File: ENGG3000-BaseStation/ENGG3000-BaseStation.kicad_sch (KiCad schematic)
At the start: 49 parts, among them J2 OLED, J3 Buttons, J4 USB_C_Receptacle_USB2.0_16P, J5 Cell 3, J6 Cell 2, J7 Cell 1, J8 CHRG LED, Q1 SS8050, Q2 AO3401A, SW1 RESET, SW2 BOOT, U1 ESP32-S3-WROOM-1-N16R8, U2 CN3085, U3 TPS63001DRCR, U5 AMS1117-3.3

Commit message: Component updates
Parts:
- removed C1: 10uF, Capacitor_SMD:C_0402_1005Metric, symbol Device:C
- removed C2, C4: 10uF, Capacitor_Tantalum_SMD:CP_EIA-3216-18_Kemet-A, symbol Device:C_Polarized
- removed R21: 1m, Resistor_SMD:R_0402_1005Metric, symbol Device:R
- removed U5: AMS1117-3.3, Package_TO_SOT_SMD:SOT-223-3_TabPin2, symbol Regulator_Linear:AMS1117-3.3
- added C10: 100nF, Capacitor_SMD:C_0402_1005Metric, symbol Device:C
- added C8, C9: 10uF, Capacitor_Tantalum_SMD:CP_EIA-3216-18_Kemet-A, symbol Device:C_Polarized
- added L1: L, Inductor_SMD:L_APV_ANR4020, symbol Device:L
- added R22: 100R, Resistor_SMD:R_0402_1005Metric, symbol Device:R
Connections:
- net +3.3V: now also U3.1 (VOUT), U3.10 (FB), C8.1, C9.1
- net GND: now also U3.11 (PGND), U3.3 (PGND), U3.9 (GND), C10.2, C8.2, C9.2
- net at U3.2 (L2): now also L1.1
- net at U3.4 (L1): now also L1.2
- net VIN: now reaches U3.5 (VIN)
- net VIN: now also R22.2
- net at U3.6 (EN): now also U3.7 (PS/SYNC), U3.8 (VINA), C10.1, R22.1
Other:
- moved on the sheet: BZ1, C3, D1, D2, D3, J2, J3, Q1, Q2, R10, R11, R12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

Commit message: Updated power path
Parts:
- added D5, D6: SS14, Diode_SMD:D_SMA, symbol Diode:SS14
- added J9: Power Switch, Connector_JST:JST_XH_B2B-XH-A_1x02_P2.50mm_Vertical, symbol Connector:Conn_01x02_Socket
- added R21: 1k, Resistor_SMD:R_0402_1005Metric, symbol Device:R
- added R23: 10k, Resistor_SMD:R_0402_1005Metric, symbol Device:R
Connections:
- net +5V: now also D6.2 (A), R21.2
- net GND: now also R23.1
- net VIN: now also D5.1 (K), D6.1 (K)
- net at C10.1, R22.1, U3.7 (PS/SYNC)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: now also J9.1 (-); no longer U3.6 (EN)
- net at Q2.1 (G): now also R21.1, R23.2
- net LATCH: no longer names the net of Q2.3 (D)
- net LATCH: now also D5.2 (A)
- new net: J9.2 (+), U3.6 (EN)
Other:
- note added: "BaseStation"
- note added: "Power path"
- note added: "Switching regulator for 3.3v"
- note removed: "Motor Driver Controller"
- moved on the sheet: BZ1, C10, C8, C9, J4, L1, Q1, Q2, R1, R2, R20, R22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

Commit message: Update to schematic
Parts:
- removed D5: SS14, Diode_SMD:D_SMA, symbol Diode:SS14
- removed J5: Cell 3, Connector_JST:JST_XH_B2B-XH-A_1x02_P2.50mm_Vertical, symbol Connector:Conn_01x02_Socket
- removed J9: Power Switch, Connector_JST:JST_XH_B2B-XH-A_1x02_P2.50mm_Vertical, symbol Connector:Conn_01x02_Socket
- removed R16: 20k, Resistor_SMD:R_0402_1005Metric, symbol Device:R
- added C8: 1uF, Capacitor_SMD:C_0402_1005Metric, symbol Device:C
- added D2: SS14, Diode_SMD:D_SMA, symbol Diode:SS14
- added J4: Power Switch, Connector_PinHeader_2.54mm:PinHeader_1x02_P2.54mm_Vertical, symbol Connector:Conn_01x02_Socket
- added J8: UltrasonicA, Connector_PinHeader_2.54mm:PinHeader_1x04_P2.54mm_Vertical, symbol Connector:Conn_01x04_Socket
- added J9: UltrasonicB, Connector_PinHeader_2.54mm:PinHeader_1x04_P2.54mm_Vertical, symbol Connector:Conn_01x04_Socket
- added R6: 10k, Resistor_SMD:R_0402_1005Metric, symbol Device:R
- J5: renamed from J2; footprint Connector_JST:JST_XH_B4B-XH-A_1x04_P2.50mm_Vertical -> Connector_PinHeader_2.54mm:PinHeader_1x04_P2.54mm_Vertical
- J6: renamed from J3; footprint (none) -> Connector_PinHeader_2.54mm:PinHeader_1x05_P2.54mm_Vertical
- L1: value L -> 2.2uH
- UART1: renamed from UART0; footprint Connector_JST:JST_XH_B4B-XH-A_1x04_P2.50mm_Vertical -> Connector_PinHeader_2.54mm:PinHeader_1x04_P2.54mm_Vertical
- renumbered C5 to C1, C3 to C2, C6 to C3, C7 to C4, C10 to C5, C9 to C6, C8 to C7, D4 to D1, D6 to D3, D1 to D4, D2 to D5, D3 to D6, J8 to J1, J6 to J2, J7 to J3, J4 to J7, Q2 to Q1, Q1 to Q2, R13 to R1, R23 to R11, R3 to R12, R11 to R13, R21 to R14, R12 to R15, R4 to R16, R22 to R17, R20 to R18, R5 to R19, R14 to R2, R1 to R20, R2 to R21, R6 to R22, R7 to R23, R8 to R3, R19 to R4, R18 to R5, R17 to R7, R15 to R8, U2 to U1, U1 to U2
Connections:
- net +3.3V: now also C8.1, J8.4 (3.3V), J9.4 (3.3V)
- net BAT: now also J2.2 (+), D2.2 (A), R6.1; no longer Q1.2 (S)
- net FB: now also R6.2
- net GND: now also C8.2, J8.1 (GND), J9.1 (GND)
- net VIN: now also J4.1 (-); no longer D3.1 (K)
- net at U3.6 (EN): now also C5.1, R17.1, U3.7 (PS/SYNC), U3.8 (VINA)
- net Ass: now reaches R23.1
- net at Q1.3 (D): now also D3.1 (K), J4.2 (+)
- new net: D2.1 (K), Q1.2 (S)
- new net GPIO12: J8.2 (TRIG)
- new net GPIO14: J8.3 (ECHO)
- new net GPIO26: J9.3 (ECHO)
- new net GPIO27: J9.2 (TRIG)
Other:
- note added: "USB-C IN"
- moved on the sheet: BZ1, D3, J7, L1, Q2, R10, R18, R20, R21, SW2

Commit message: Sensor Calibration
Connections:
- net Ass is gone; now on net GPIO14: R23.1
- net GPIO12 is gone; now on net GPIO1: J8.2 (TRIG)
- net GPIO26 is gone; now on net GPIO13: J9.3 (ECHO)
- net GPIO27 is gone; now on net GPIO4: J9.2 (TRIG)
- net GPIO14: now also U2.22 (GPIO14/TOUCH14/ADC2_CH3/FSPIWP/FSPIDQS/SUBSPIWP); no longer J8.3 (ECHO)
- net GPIO6: now reaches J6.2 (Button_A)
- net GPIO6: now also U2.6 (GPIO6/TOUCH6/ADC1_CH5)
- net GPIO7: now reaches J6.3 (Button_B)
- net GPIO7: now also U2.7 (GPIO7/TOUCH7/ADC1_CH6)
- net GPIO10: now reaches J6.4 (Button_C)
- net GPIO10: now also U2.18 (GPIO10/TOUCH10/ADC1_CH9/FSPICS0/FSPIIO4/SUBSPICS0)
- net GPIO11: now reaches J6.5 (Button_D)
- net GPIO11: now also U2.19 (GPIO11/TOUCH11/ADC2_CH0/FSPID/FSPIIO5/SUBSPID)
- net GPIO17: now reaches R18.1
- net GPIO17: now also U2.10 (GPIO17/U1TXD/ADC2_CH6)
- net GPIO3: now reaches U2.15 (GPIO3/TOUCH3/ADC1_CH2)
- net GPIO3: now also J8.3 (ECHO)
- net GPIO13: now reaches U2.21 (GPIO13/TOUCH13/ADC2_CH2/FSPIQ/FSPIIO7/SUBSPIQ)
- net GPIO1: now reaches U2.39 (GPIO1/TOUCH1/ADC1_CH0)
- net GPIO4: now reaches U2.4 (GPIO4/TOUCH4/ADC1_CH3)
- no-connect marks 5 -> 8

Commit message: Kicad footprint update
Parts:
- removed C4: 10uF, Capacitor_SMD:C_0402_1005Metric, symbol Device:C
- removed D2: SS14, Diode_SMD:D_SMA, symbol Diode:SS14
- removed J1: CHRG LED, Connector_JST:JST_XH_B2B-XH-A_1x02_P2.50mm_Vertical, symbol Connector:Conn_01x02_Socket
- removed R7: 10k, Resistor_SMD:R_0402_1005Metric, symbol Device:R
- removed R8: 5.1k, Resistor_SMD:R_0402_1005Metric, symbol Device:R
- added C5, C9: 10uF, Capacitor_SMD:C_0805_2012Metric, symbol Device:C
- added J8: Cell 3, Connector_JST:JST_XH_B2B-XH-A_1x02_P2.50mm_Vertical, symbol Connector:Conn_01x02_Socket
- added JP1, JP2: SolderJumper, Jumper:SolderJumper-2_P1.3mm_Bridged2Bar_RoundedPad1.0x1.5mm, symbol Jumper:SolderJumper_2_Bridged
- added R23: 10k, Resistor_SMD:R_0805_2012Metric_Pad1.20x1.40mm_HandSolder, symbol Device:R
- C8: renamed from C3; footprint Capacitor_SMD:C_0402_1005Metric -> Capacitor_SMD:C_0805_2012Metric; LCSC part C15525 -> C15850
- D5: renamed from D3; LCSC part (none) -> C2480
- J10: renamed from J3; value Cell 1 -> Cell/Pack 1
- R20: renamed from R6; footprint Resistor_SMD:R_0402_1005Metric -> Resistor_SMD:R_0805_2012Metric_Pad1.20x1.40mm_HandSolder; LCSC part C25744 -> C17414
- renumbered C2 to C1, C6 to C2, C7 to C3, C8 to C4, C5 to C6, C1 to C7, D4 to D1, D5 to D2, D6 to D3, D1 to D4, J5 to J1, J6 to J2, J8 to J3, J9 to J4, J7 to J5, J4 to J7, J2 to J9, Q2 to Q1, Q1 to Q2, R3 to R1, R20 to R10, R21 to R11, R18 to R12, R17 to R13, R4 to R14, R5 to R15, R9 to R17, R11 to R18, R1 to R19, R19 to R2, R14 to R21, R2 to R22, R22 to R3, R23 to R4, R12 to R5, R16 to R6, R10 to R7, R13 to R8, R15 to R9, U2 to U1, U3 to U2, U1 to U3
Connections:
- net +5V: now also R21.1; no longer R21.2
- net BAT: now also Q2.3 (D), J8.2 (+), JP1.1 (A); no longer J9.2 (+)
- net FB: now also R23.1
- net GND: now also C5.2, C9.2, R23.2
- net VIN: now also C5.1
- net at D5.1 (K), J7.2 (+): now also Q2.2 (S); no longer Q2.3 (D)
- net at Q2.1 (G), R18.2: now also R21.2; no longer R21.1
- net at R15.2, U3.6 (RC): now also C9.1
- net at J10.2 (+), J9.1 (-): now also JP2.1 (A)
- new net: J8.1 (-), J9.2 (+), JP1.2 (B), JP2.2 (B)
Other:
- moved on the sheet: C6, D5, J10, J7, J9, Q2, R13, R18, R21

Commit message: PCB footprint addition and Calibration graphs added
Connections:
- net +3.3V: now also BZ1.1 (+)
- net +5V: no longer BZ1.1 (+)
- net GPIO1: now also J2.2 (Button_A); no longer J3.2 (TRIG)
- net GPIO10: now also J4.3 (ECHO); no longer J2.4 (Button_C)
- net GPIO11: now also J3.3 (ECHO); no longer J2.5 (Button_D)
- net GPIO13: now also J3.2 (TRIG); no longer J4.3 (ECHO)
- net GPIO3: now also J4.2 (TRIG); no longer J3.3 (ECHO)
- net GPIO48: now reaches U1.25 (GPIO48/SPICLK_N/SUBSPICLK_N_DIFF)
- net GPIO48: now also R4.1
- net GPIO40: now reaches U1.33 (MTDO/GPIO40/CLK_OUT2)
- net GPIO40: now also J2.5 (Button_D)
- net GPIO41: now reaches U1.34 (MTDI/GPIO41/CLK_OUT1)
- net GPIO41: now also J2.4 (Button_C)
- net GPIO43: now reaches U1.35 (MTMS/GPIO42)
- net GPIO43: now also J2.3 (Button_B)
- net GPIO14: no longer names the net of U1.22 (GPIO14/TOUCH14/ADC2_CH3/FSPIWP/FSPIDQS/SUBSPIWP)
- net GPIO14: no longer R4.1
- net GPIO4: no longer names the net of U1.4 (GPIO4/TOUCH4/ADC1_CH3)
- net GPIO4: no longer J4.2 (TRIG)
- net GPIO6: no longer names the net of U1.6 (GPIO6/TOUCH6/ADC1_CH5)
- net GPIO6: no longer J2.2 (Button_A)
- net GPIO7: no longer names the net of U1.7 (GPIO7/TOUCH7/ADC1_CH6)
- net GPIO7: no longer J2.3 (Button_B)

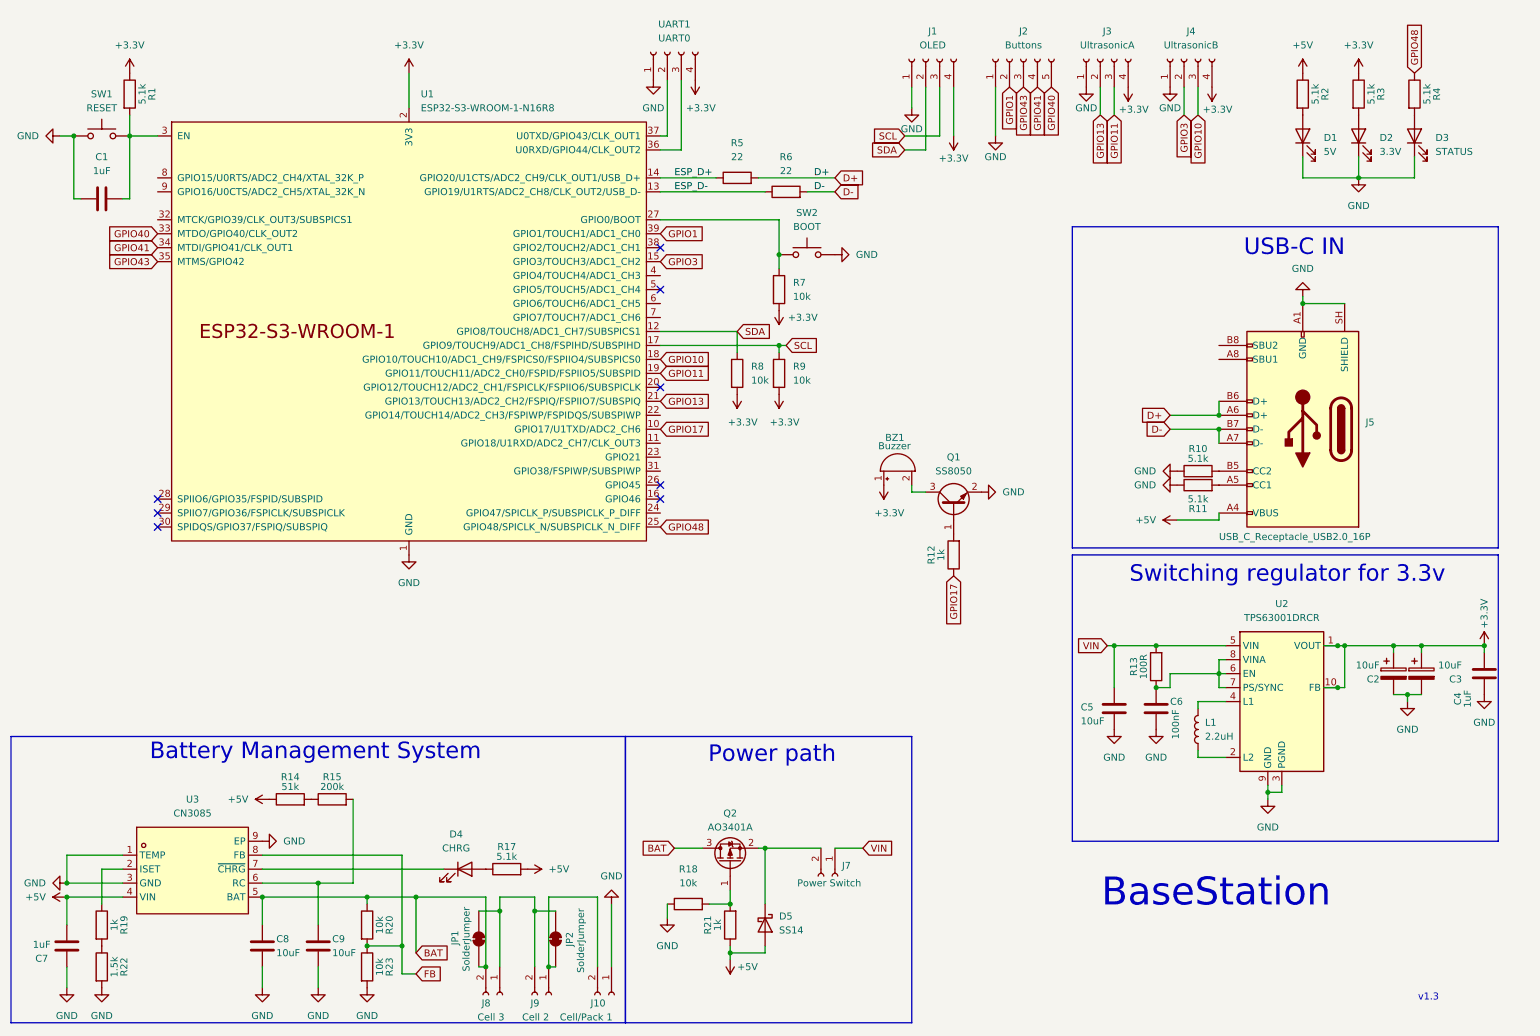
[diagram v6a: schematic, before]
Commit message: 4 cell and linear reg setup
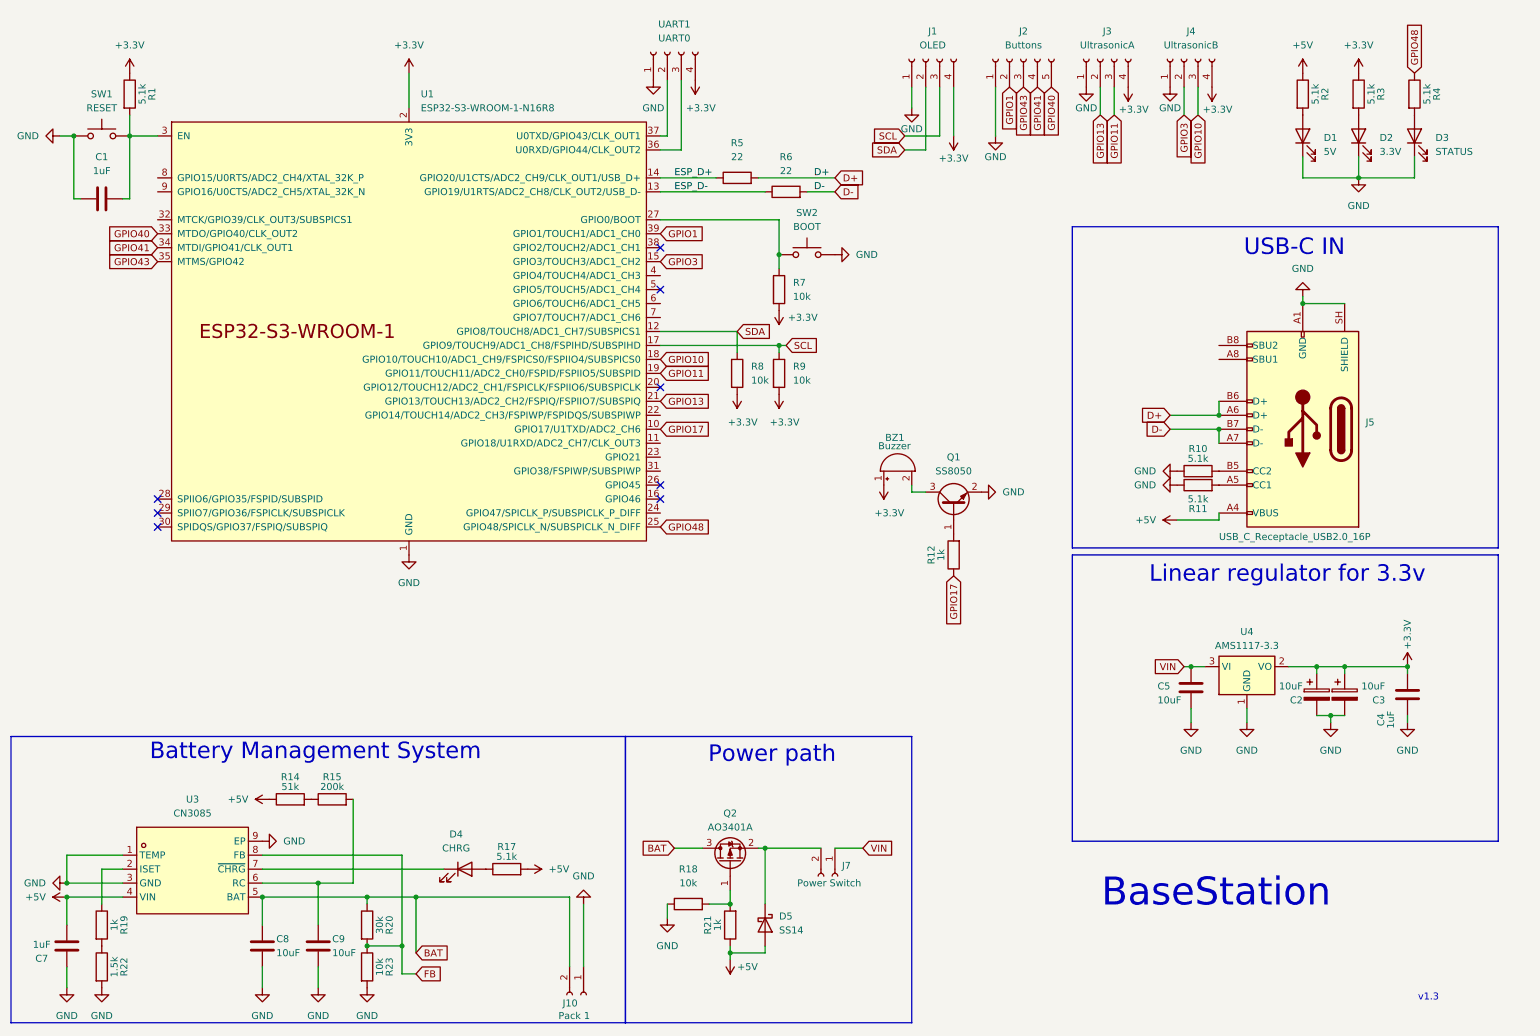
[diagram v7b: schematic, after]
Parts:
- removed C6: 100nF, Capacitor_SMD:C_0402_1005Metric, symbol Device:C
- removed J8: Cell 3, Connector_JST:JST_XH_B2B-XH-A_1x02_P2.50mm_Vertical, symbol Connector:Conn_01x02_Socket
- removed J9: Cell 2, Connector_JST:JST_XH_B2B-XH-A_1x02_P2.50mm_Vertical, symbol Connector:Conn_01x02_Socket
- removed JP1, JP2: SolderJumper, Jumper:SolderJumper-2_P1.3mm_Bridged2Bar_RoundedPad1.0x1.5mm, symbol Jumper:SolderJumper_2_Bridged
- removed L1: 2.2uH, Inductor_SMD:L_APV_ANR4020, symbol Device:L
- removed R13: 100R, Resistor_SMD:R_0402_1005Metric, symbol Device:R
- removed U2: TPS63001DRCR, Package_SON:Texas_DRC0010J_ThermalVias, symbol Regulator_Switching:TPS63001
- added U4: AMS1117-3.3, Package_TO_SOT_SMD:SOT-223-3_TabPin2, symbol Regulator_Linear:AMS1117-3.3
- J10: value Cell/Pack 1 -> Pack 1
- R20: value 10k -> 30k; LCSC part C17414 -> C17621
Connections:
- net +3.3V: now also U4.2 (VO)
- net BAT: now also J10.2 (+)
- net GND: now also U4.1 (GND)
- net VIN: now also U4.3 (VI)
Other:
- note added: "Linear regulator for 3.3v"
- note removed: "Switching regulator for 3.3v"
- moved on the sheet: C2, C3, C4, C5, J10
